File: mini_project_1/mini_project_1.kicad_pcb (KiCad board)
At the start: 2 copper layers, 23.5 x 15 mm, 14 parts, among them J1 480370001, U2 MCP1700x-330xxTT, U3 MCP6021

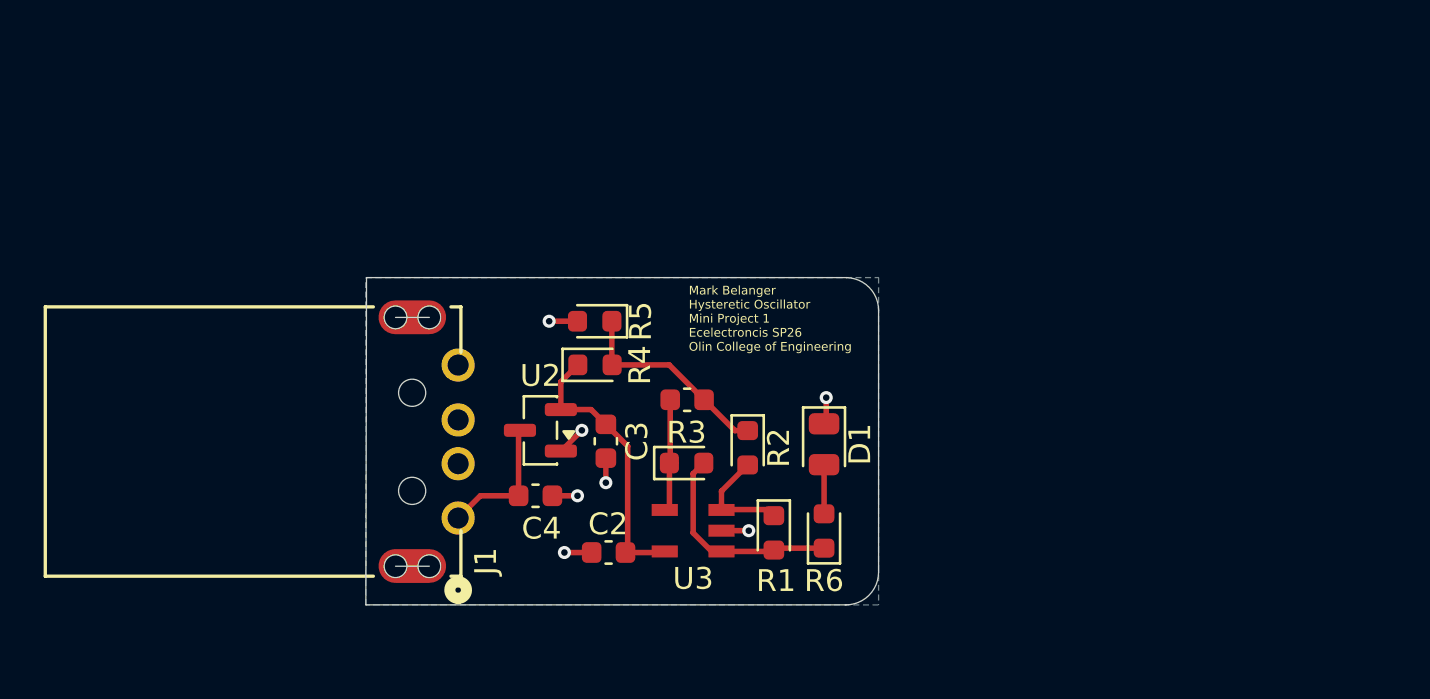
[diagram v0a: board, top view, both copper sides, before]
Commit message: Use op amp buffer for 1.65V net
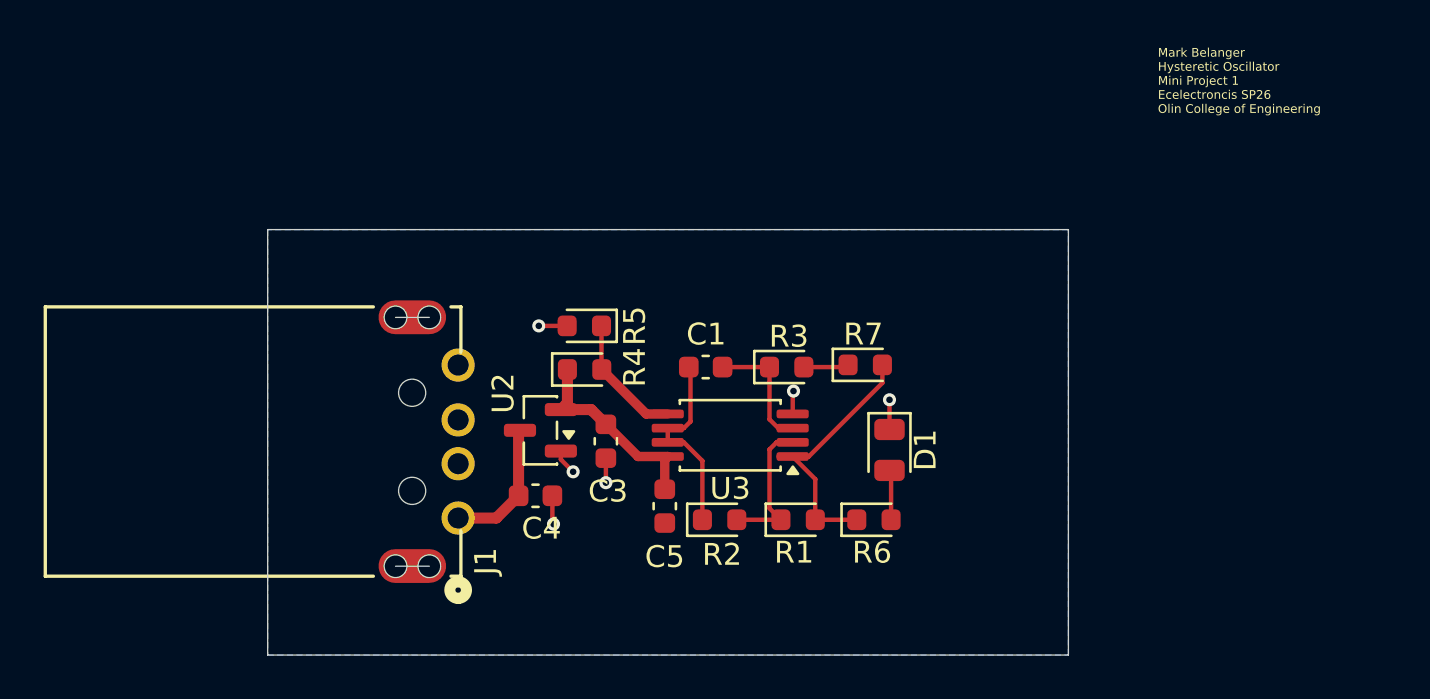
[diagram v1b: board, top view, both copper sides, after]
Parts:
- removed C2: 0.1u, Capacitor_SMD:C_0603_1608Metric
- added C5: 0.1u, Capacitor_SMD:C_0603_1608Metric, F.Cu at (148.2, 104.0)
- added R7: 1k, Diode_SMD:D_0603_1608Metric, F.Cu at (157.4, 97.5)
- R4, R5: value R_US -> 1k
- R6: value 301 -> 1k
- U3: value MCP6021 -> MCP602; footprint MCP6021:SOT23-5 -> Package_SO:TSSOP-8_4.4x3mm_P0.65mm
- moved R3 6.36 mm to (153.8, 97.6)
- moved U3 4.69 mm to (151.2, 100.7), turned to 180 degrees
- moved R2 3.54 mm to (150.7, 104.6), turned to 0 degrees
- moved D1 3.01 mm to (158.5, 101.4)
- moved R6 2.34 mm to (157.8, 104.6), turned to 0 degrees
- moved C1 1.72 mm to (150.1, 97.6), turned to 180 degrees
- moved R1 1.26 mm to (154.3, 104.6), turned to 0 degrees
- moved R5 0.52 mm to (144.5, 95.7)
- moved R4 0.52 mm to (144.5, 97.7)
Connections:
- C1 pad 1: Net-(C1-Pad1) -> Net-(U3A-+)
- R1 pad 1: Net-(R1-Pad1) -> Net-(U3A--)
- R2 pad 2: Net-(R1-Pad1) -> Net-(U3A--)
- R3 pad 1: Net-(C1-Pad1) -> Net-(U3A-+)
- R3 pad 2: Net-(R1-Pad2) -> Net-(R3-Pad2)
- R4 pad 2: /+1.65 -> Net-(U3B-+)
- R5 pad 1: /+1.65 -> Net-(U3B-+)
- U3 pad 2: GND -> Net-(U3A--)
- U3 pad 3: Net-(R1-Pad1) -> Net-(U3A-+)
- U3 pad 4: Net-(C1-Pad1) -> GND
- U3 pad 5: +3.3V -> Net-(U3B-+)
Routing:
- net Net-(U3A--): track 0.00 -> 6.67 mm
- net Net-(U3B-+): track 0.00 -> 6.19 mm
- net Net-(U3A-+): track 0.00 -> 5.78 mm
- net Net-(C1-Pad1): track 5.52 -> 0.00 mm
- net Net-(R1-Pad1): track 5.18 -> 0.00 mm
- net +3.3V: track 12.9 -> 9.31 mm
- net Net-(R1-Pad2): track 9.92 -> 12.2 mm
- net Net-(R3-Pad2): track 0.00 -> 2.07 mm
- net GND: track 8.63 -> 7.36 mm, vias 7 -> 6
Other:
- board size 23.5 x 15 mm -> 36.7 x 19.5 mm

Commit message: Modify schematic, layout, and add report
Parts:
- added R5: 499k, Resistor_SMD:R_0603_1608Metric, F.Cu at (157.5, 99.4)
- added R6: 49.9k, Resistor_SMD:R_0603_1608Metric, F.Cu at (157.6, 101.2)
- C1: value 1u -> 0.1u
- R1, R2: footprint Diode_SMD:D_0603_1608Metric -> Resistor_SMD:R_0603_1608Metric
- R3: value 499k -> 2M; footprint Diode_SMD:D_0603_1608Metric -> Resistor_SMD:R_0603_1608Metric
- R4: renamed from R7; value 1k -> 2M; footprint Diode_SMD:D_0603_1608Metric -> Resistor_SMD:R_0603_1608Metric
- R7: renamed from R4; footprint Diode_SMD:D_0603_1608Metric -> Resistor_SMD:R_0603_1608Metric
- R8: renamed from R5; footprint Diode_SMD:D_0603_1608Metric -> Resistor_SMD:R_0603_1608Metric
- R9: renamed from R6; footprint Diode_SMD:D_0603_1608Metric -> Resistor_SMD:R_0603_1608Metric
- moved D1 2.68 mm to (159.3, 104.0), turned to 90 degrees
- moved R9 1.19 mm to (156.9, 103.8), turned to 90 degrees
- moved R4 0.22 mm to (157.6, 97.6)
- moved C4 0.10 mm to (148.2, 104.1)
- renumbered C4 to C2, C5 to C4
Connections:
- R4 pad 2: Net-(R1-Pad2) -> Net-(R4-Pad2)
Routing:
- net Net-(R1-Pad2): track 12.2 -> 9.47 mm
- net Net-(R5-Pad2): track 0.00 -> 2.48 mm
- net Net-(R4-Pad2): track 0.00 -> 1.83 mm
- net GND: track 7.36 -> 8.87 mm, vias 6 -> 7
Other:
- board size 36.7 x 19.5 mm -> 26.4 x 14.3 mm

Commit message: Add complete schematic, layout, report, sim
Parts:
- moved R4 1.52 mm to (156.1, 97.7)
- moved R1 1.42 mm to (153.2, 103.7)
- moved R2 1.42 mm to (149.6, 103.7)
- moved R5 1.42 mm to (156.1, 99.5)
- moved R6 1.42 mm to (156.2, 101.3)
- moved R7 1.37 mm to (144.1, 99.0)
- moved R8 1.37 mm to (144.1, 97.0)
- moved C2 1.34 mm to (141.8, 104.8)
- moved U2 1.34 mm to (142.1, 101.8)
- moved D1 1.30 mm to (158.0, 104.1)
- moved R9 1.03 mm to (155.9, 103.9)
- moved C1 1.03 mm to (149.1, 97.7)
- moved R3 1.03 mm to (152.8, 97.7)
- moved U3 1.03 mm to (150.2, 100.8)
- moved C4 1.03 mm to (147.2, 104.2)
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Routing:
- net +3.3V: track 9.31 -> 8.00 mm
- net Net-(U3B-+): track 5.89 -> 4.74 mm
- net /+1.65: track 8.98 -> 7.93 mm
- net GND: track 8.87 -> 7.85 mm
- net Net-(R1-Pad2): track 9.47 -> 8.51 mm
- net Net-(J1-VBUS): track 6.22 -> 5.47 mm
- net Net-(R3-Pad2): track 2.23 -> 1.66 mm
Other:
- board size 26.4 x 14.3 mm -> 25.2 x 14.3 mm

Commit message: Final layout changes
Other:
- board text added: "Mark Belanger Hysteretic Oscillator Mini Project 1 Ecelectroncis SP26 Olin College of Engineering 09 February 2026"
- board text removed: "Mark Belanger Hysteretic Oscillator Mini Project 1 Ecelectroncis SP26 Olin College of Engineering"
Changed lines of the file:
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@@
 		(layer "Edge.Cuts")
 	)
-	(gr_text "Mark Belanger\nHysteretic Oscillator\nMini Project 1\nEcelectroncis SP26\nOlin College of Engineering"
-		(at 158.7 102.3 0)
+	(gr_text "Mark Belanger\nHysteretic Oscillator\nMini Project 1\nEcelectroncis SP26\nOlin College of Engineering\n09 February 2026"
+		(at 158.8 103.8 0)
 		(layer "B.SilkS")
 		(effects
